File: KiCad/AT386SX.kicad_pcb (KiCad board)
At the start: 2 copper layers, 218.4 x 167.6 mm, 145 parts, among them J1 KEYBOARD, J10 OSC_PIN1, J11 OSC_PIN8, J2 BUSAT_HOST, J3 BUSAT_HOST, J4 BUSAT_HOST, J5 BUSAT_HOST, J6 BUSAT_HOST, J7 BUSAT_HOST, J8 AT_POWER1, J9 AT_POWER2, Q1 2N3906, Q2 2N3904, Q3 2N3904, U1 8242KBD, U10 SIMM0, U11 SIMM1, U12 SIMM2, U13 SIMM3, U2 74HC05, U3 27C512, U4 HM6818A, U5 4069, U6 ICW42C07, U7 Cx486SLC, U8 80387SX, U9 RC2016A5, X1 32768Hz, X2 14.31818MHz

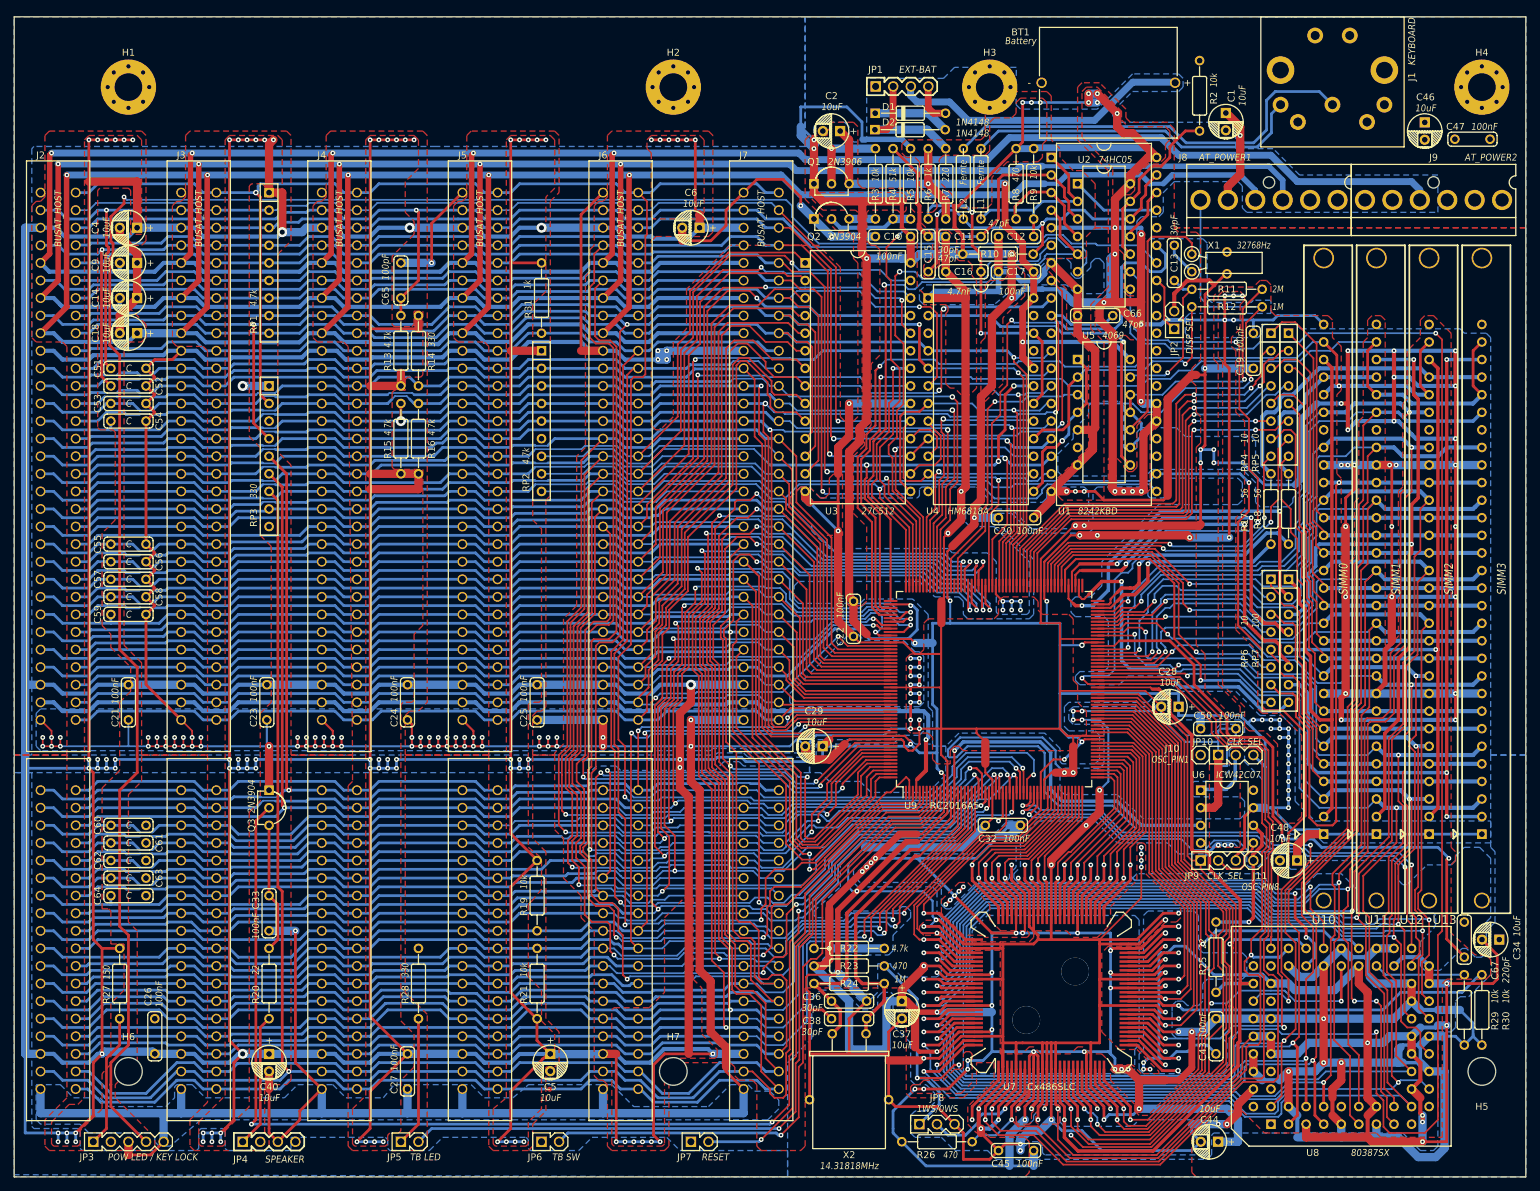
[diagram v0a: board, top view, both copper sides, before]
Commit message: Add R32, update footprints
Signed-off-by: Sergey Kiselev <skiselev@gmail.com>
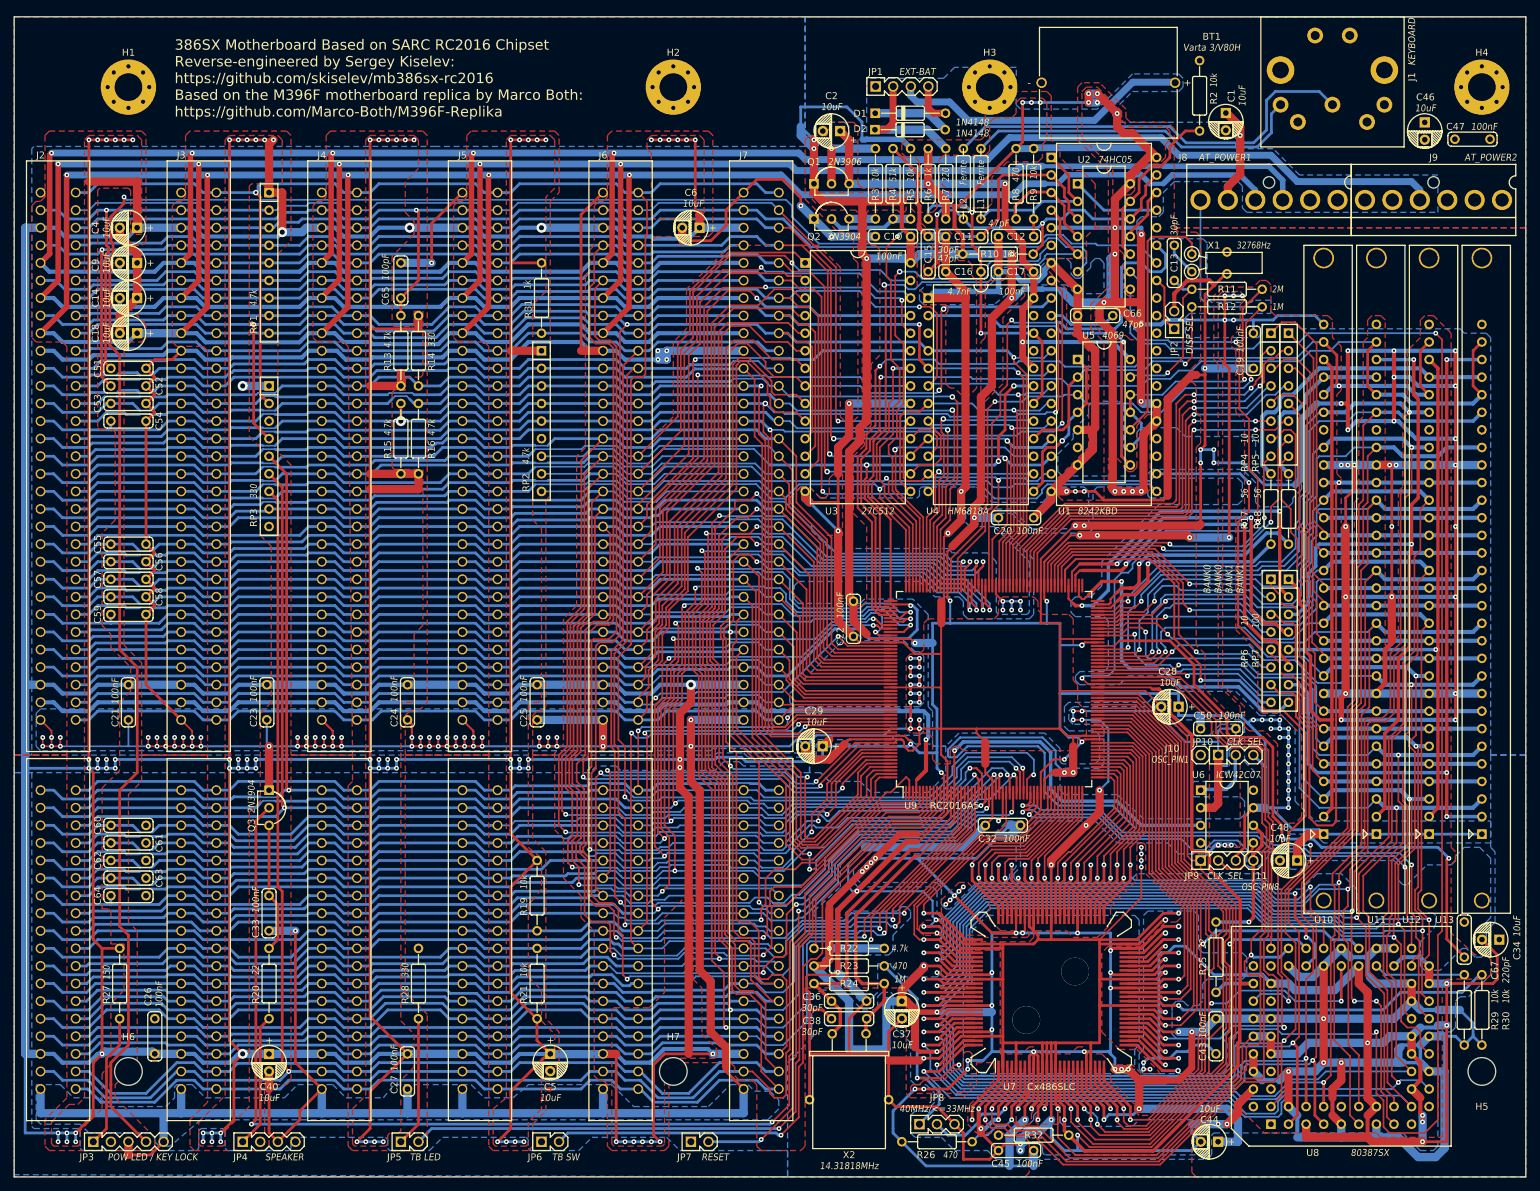
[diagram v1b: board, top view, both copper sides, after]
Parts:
- added R32: DNP, My_Components:Res_Axial_L6.3mm_D2.5mm_P10.16mm_Horizontal, F.Cu at (162.6, 174.3)
- BT1: value Battery -> Varta 3/V80H
- JP8: value 1WS/0WS -> 40MHz/<=33MHz
- U10: value SIMM0 -> BANK0
- U11: value SIMM1 -> BANK0
- U12: value SIMM2 -> BANK1
- U13: value SIMM3 -> BANK1
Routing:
- net GND: track 2561.0 -> 2563.6 mm
- net CLK2: track 118.5 -> 117.9 mm
- net ~{BLE}: track 100.7 -> 100.1 mm
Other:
- board text added: "386SX Motherboard Based on SARC RC2016 Chipset Reverse-engineered by Sergey Kiselev: https://github.com/skiselev/mb386sx-rc2016 Based on the M396F motherboard replica by Marco Both: https://github.com/Marco-Both/M396F-Replika"

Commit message: Use DS12885 RTC
Signed-off-by: Sergey Kiselev <skiselev@gmail.com>
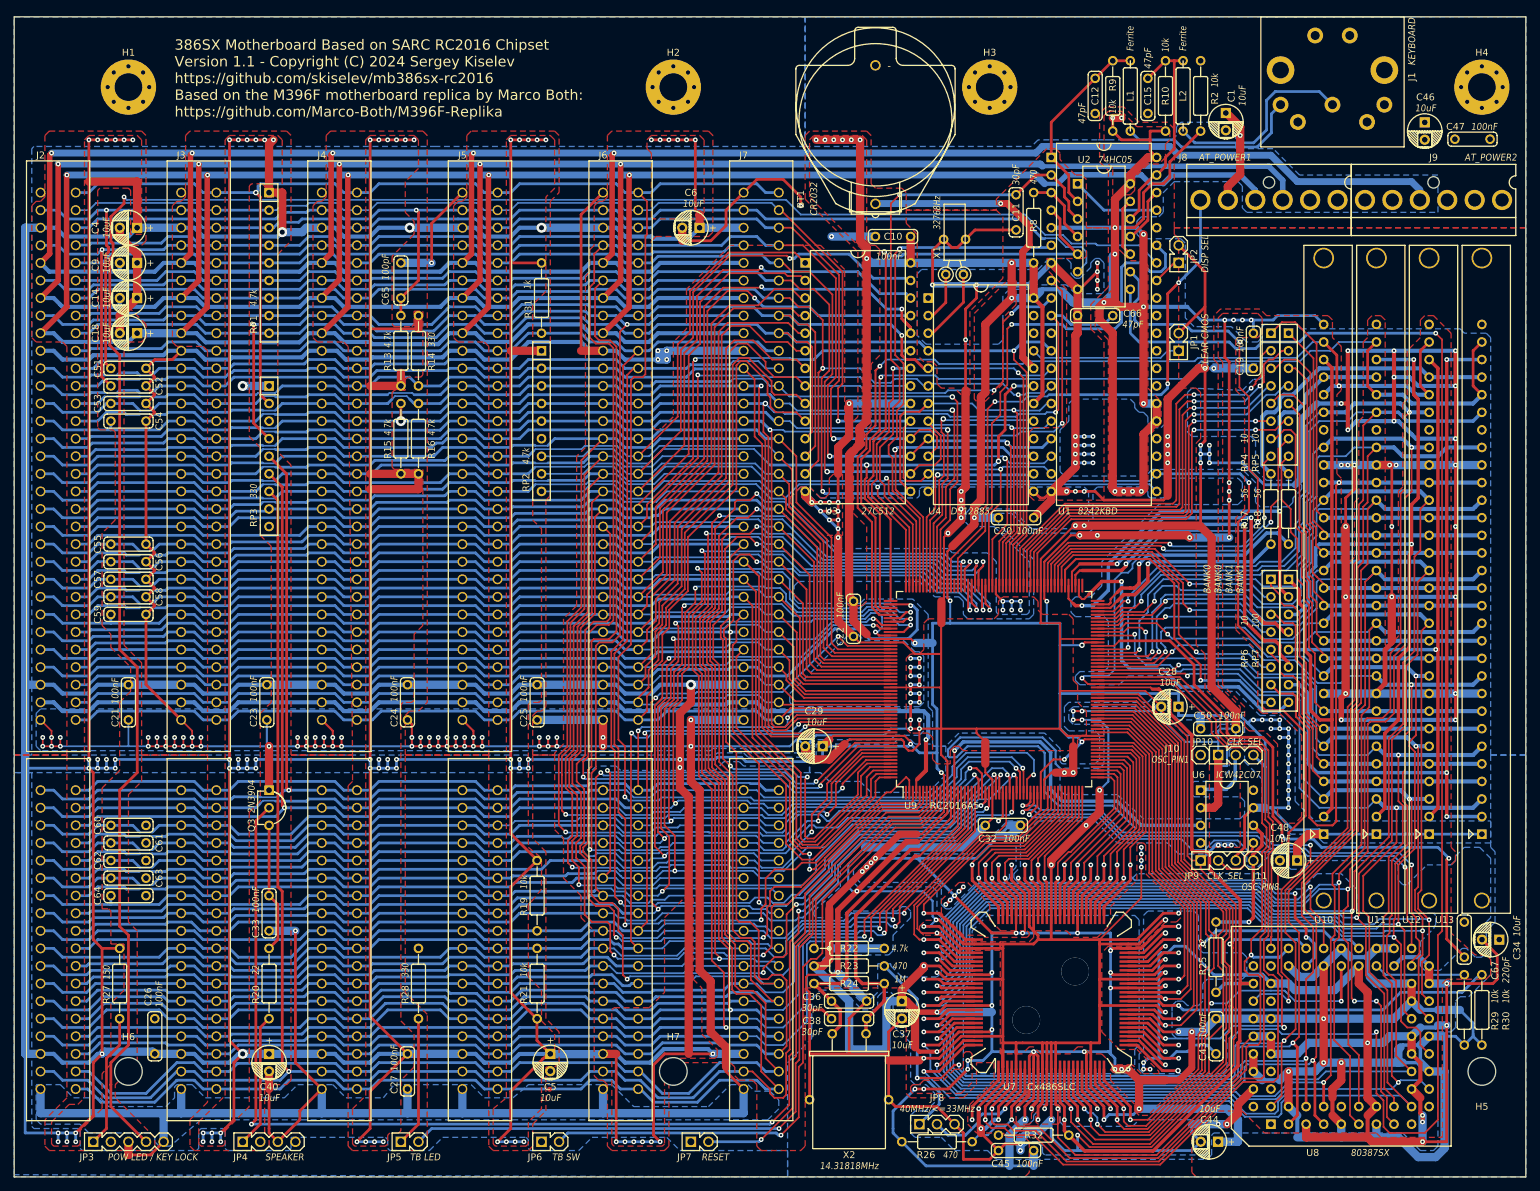
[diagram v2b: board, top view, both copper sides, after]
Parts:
- removed C13: 30pF, My_Components:Cap_Cer_508
- removed C16: 4.7nF, My_Components:Cap_Cer_508
- removed C17: 100nF, My_Components:Cap_Cer_508
- removed C2: 10uF, My_Components:Cap_Elec_Radial_5mm_2.5mm
- removed D1, D2: 1N4148, My_Components:Diode_1016
- removed Q1: 2N3906, My_Components:Transistor_TO92_EBC_254
- removed Q2: 2N3904, My_Components:Transistor_TO92_EBC_254
- removed R11: 2M, My_Components:Res_Axial_L6.3mm_D2.5mm_P10.16mm_Horizontal
- removed R12: 1M, My_Components:Res_Axial_L6.3mm_D2.5mm_P10.16mm_Horizontal
- removed R3, R4: 10k, My_Components:Res_Axial_L6.3mm_D2.5mm_P10.16mm_Horizontal
- removed R5: 51k, My_Components:Res_Axial_L6.3mm_D2.5mm_P10.16mm_Horizontal
- removed R6: 1k, My_Components:Res_Axial_L6.3mm_D2.5mm_P10.16mm_Horizontal
- removed R7: 220, My_Components:Res_Axial_L6.3mm_D2.5mm_P10.16mm_Horizontal
- removed U5: 4069, My_Components:IC_DIP14_300
- BT1: value Varta 3/V80H -> CR2032; footprint My_Components:Battery_Varta_3V80H -> My_Components:Battery_Holder_CR2032_Universal
- JP1: value EXT-BAT -> CLEAR CMOS; footprint My_Components:Conn_Pin_Header_4x1_2.54mm -> My_Components:Conn_Pin_Header_2x1_2.54mm
- U4: value HM6818A -> DS12885
- moved JP1 54.4 mm to (183.5, 59.7), turned to 90 degrees
- moved C15 39.1 mm to (179.1, 24.1), turned to -90 degrees
- moved X1 34.3 mm to (151.1, 49.9), turned to 180 degrees
- moved L2 34.2 mm to (184.2, 24.1), turned to -90 degrees
- moved BT1 33.8 mm to (139.7, 25.7), turned to 90 degrees
- moved R10 33.3 mm to (181.6, 24.1), turned to 90 degrees
- moved L1 25.0 mm to (176.5, 24.1), turned to -90 degrees
- moved C12 23.3 mm to (171.4, 24.1), turned to -90 degrees
- moved R9 17.1 mm to (174.0, 24.1), turned to 90 degrees
- moved JP2 9.55 mm to (183.5, 47.0)
- moved C11 8.38 mm to (160.0, 41.0), turned to -90 degrees
- moved R8 6.84 mm to (162.6, 43.2), turned to 90 degrees
- moved R2 0.15 mm to (186.7, 24.1)
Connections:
- JP1 pad 1: GND -> Net-(JP1-Pad1)
- JP1 pad 2: Net-(D2-Pad1) -> GND
- U4 pad 1: GND -> unconnected-(U4-Pad1)
- U4 pad 13: Net-(U4-Pad13) -> GND
- U4 pad 16: Net-(R12-Pad2) -> GND
- U4 pad 18: Net-(C16-Pad1) -> VCC
- U4 pad 20: Net-(C17-Pad1) -> Net-(BT1-Pad1)
- U4 pad 21: unconnected-(U4-Pad21) -> Net-(JP1-Pad1)
- U4 pad 22: Net-(C16-Pad1) -> unconnected-(U4-Pad22)
- U4 pad 24: Net-(C17-Pad1) -> VCC
- U4 pad 3: unconnected-(U4-Pad3) -> Net-(U4-Pad3)
- X1 pad 1: Net-(C13-Pad2) -> Net-(U4-Pad3)
- X1 pad 2: Net-(U5-Pad10) -> Net-(U4-Pad2)
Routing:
- net VCC: track 2902.1 -> 2812.6 mm
- net Net-(C17-Pad1): track 88.2 -> 0.00 mm, vias 3 -> 0
- net Net-(C16-Pad1): track 45.1 -> 0.00 mm, vias 2 -> 0
- net Net-(U4-Pad2): track 48.3 -> 7.37 mm, vias 1 -> 0
- net Net-(R11-Pad1): track 40.7 -> 0.00 mm, vias 1 -> 0
- net Net-(R12-Pad2): track 38.6 -> 0.00 mm, vias 1 -> 0
- net Net-(U5-Pad10): track 36.7 -> 0.00 mm
- net Net-(J1-Pad2): track 62.0 -> 28.7 mm
- net GND: track 2563.6 -> 2591.0 mm, vias 180 -> 219
- net Net-(U4-Pad13): track 23.5 -> 0.00 mm, vias 1 -> 0
- net Net-(J1-Pad1): track 49.4 -> 26.8 mm
- net Net-(C13-Pad1): track 22.5 -> 0.00 mm, vias 1 -> 0
- net Net-(JP1-Pad1): track 0.00 -> 21.8 mm
- net POWER_GOOD: track 105.2 -> 84.2 mm, vias 2 -> 3
- net Net-(C15-Pad1): track 52.5 -> 31.8 mm, vias 2 -> 0
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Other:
- board text added: "386SX Motherboard Based on SARC RC2016 Chipset Version 1.1 - Copyright (C) 2024 Sergey Kiselev https://github.com/skiselev/mb386sx-rc2016 Based on the M396F motherboard replica by Marco Both: https://github.com/Marco-Both/M396F-Replika"
- board text removed: "386SX Motherboard Based on SARC RC2016 Chipset Reverse-engineered by Sergey Kiselev: https://github.com/skiselev/mb386sx-rc2016 Based on the M396F motherboard replica by Marco Both: https://github.com/Marco-Both/M396F-Replika"

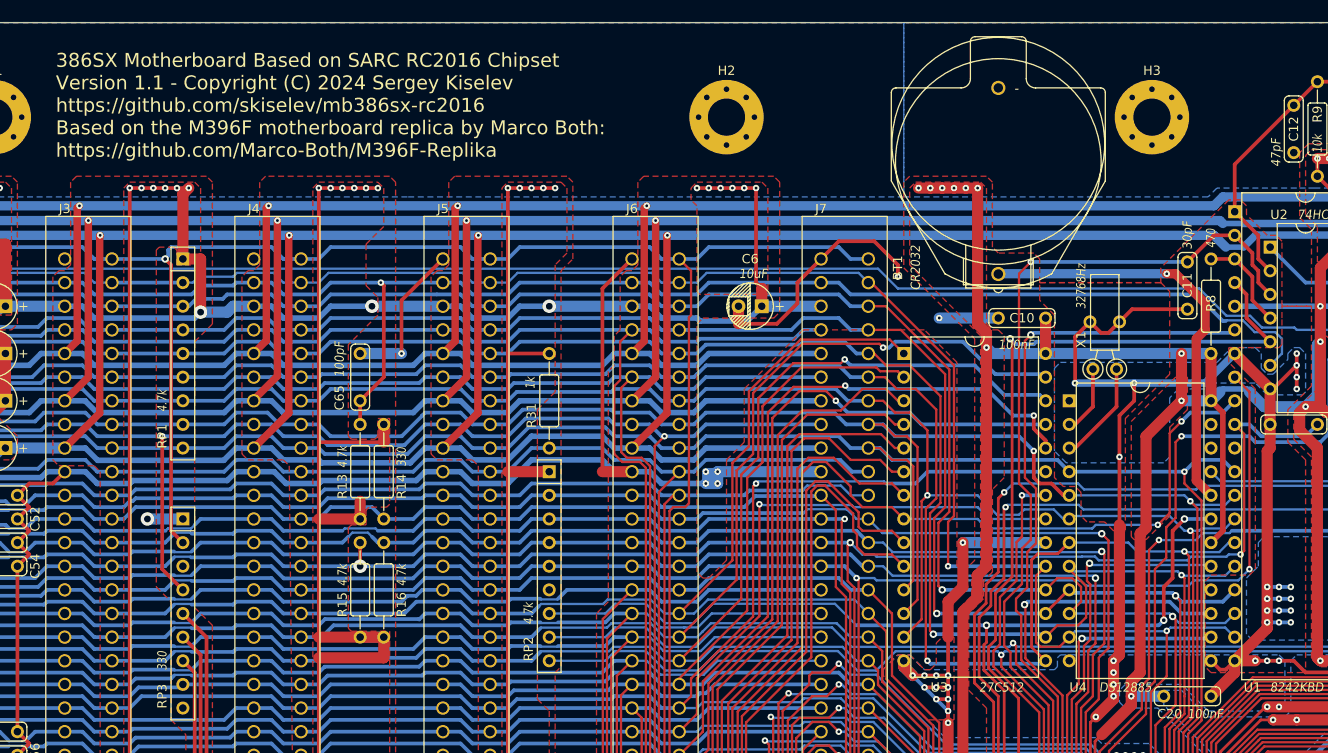
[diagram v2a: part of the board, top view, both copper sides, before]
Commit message: Add support for 128 KiB Flash ROM ICs
Signed-off-by: Sergey Kiselev <skiselev@gmail.com>
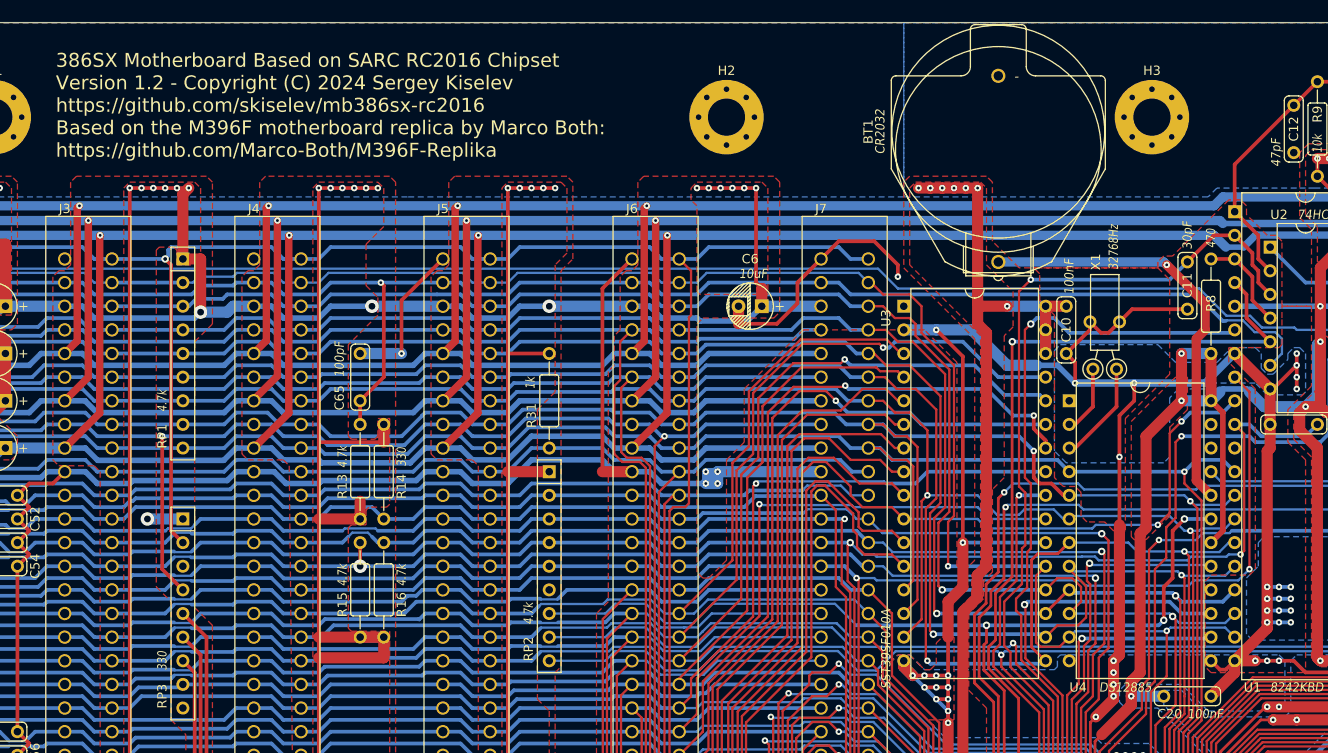
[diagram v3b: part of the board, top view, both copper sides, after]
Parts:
- U3: value 27C512 -> SST39SF010A; footprint My_Components:IC_DIP28_600 -> My_Components:IC_DIP32_600
- moved C10 4.93 mm to (147.0, 45.7), turned to -90 degrees
- moved U3 2.54 mm to (137.2, 62.2)
- moved BT1 1.30 mm to (139.7, 24.4)
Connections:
- U3 pad 1: SA15 -> unconnected-(U3-Pad1)
- U3 pad 10: SA0 -> SA2
- U3 pad 11: SD0 -> SA1
- U3 pad 12: SD1 -> SA0
- U3 pad 13: SD2 -> SD0
- U3 pad 14: GND -> SD1
- U3 pad 15: SD3 -> SD2
- U3 pad 16: SD4 -> GND
- U3 pad 17: SD5 -> SD3
- U3 pad 18: SD6 -> SD4
- U3 pad 19: SD7 -> SD5
- U3 pad 2: SA12 -> GND
- U3 pad 20: GND -> SD6
- U3 pad 21: SA10 -> SD7
- U3 pad 22: ~{BIOS_RD} -> GND
- U3 pad 23: SA11 -> SA10
- U3 pad 24: SA9 -> ~{BIOS_RD}
- U3 pad 25: SA8 -> SA11
- U3 pad 26: SA13 -> SA9
- U3 pad 27: SA14 -> SA8
- U3 pad 28: VCC -> SA13
- U3 pad 3: SA7 -> SA15
- U3 pad 4: SA6 -> SA12
- U3 pad 5: SA5 -> SA7
- U3 pad 6: SA4 -> SA6
- U3 pad 7: SA3 -> SA5
- U3 pad 8: SA2 -> SA4
- U3 pad 9: SA1 -> SA3
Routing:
- net GND: track 2591.0 -> 2630.3 mm
- net VCC: track 2812.6 -> 2802.3 mm
- net SD7: track 200.1 -> 201.8 mm
- net KBC_CLK: track 91.7 -> 90.1 mm
- net ~{KBC_CS}: track 74.3 -> 75.8 mm
- net ~{RESET}: track 89.1 -> 88.1 mm
- net SD6: track 200.0 -> 200.7 mm
- net Net-(BT1-Pad1): track 45.2 -> 45.8 mm
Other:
- board text added: "386SX Motherboard Based on SARC RC2016 Chipset Version 1.2 - Copyright (C) 2024 Sergey Kiselev https://github.com/skiselev/mb386sx-rc2016 Based on the M396F motherboard replica by Marco Both: https://github.com/Marco-Both/M396F-Replika"
- board text added: "ATX I/O Area"
- board text removed: "386SX Motherboard Based on SARC RC2016 Chipset Version 1.1 - Copyright (C) 2024 Sergey Kiselev https://github.com/skiselev/mb386sx-rc2016 Based on the M396F motherboard replica by Marco Both: https://github.com/Marco-Both/M396F-Replika"
